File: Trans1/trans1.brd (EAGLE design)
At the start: 45.7 x 33 mm, 21 parts, among them Q1 MOSFET-NCHANNELBSS138, U1 DRA818V

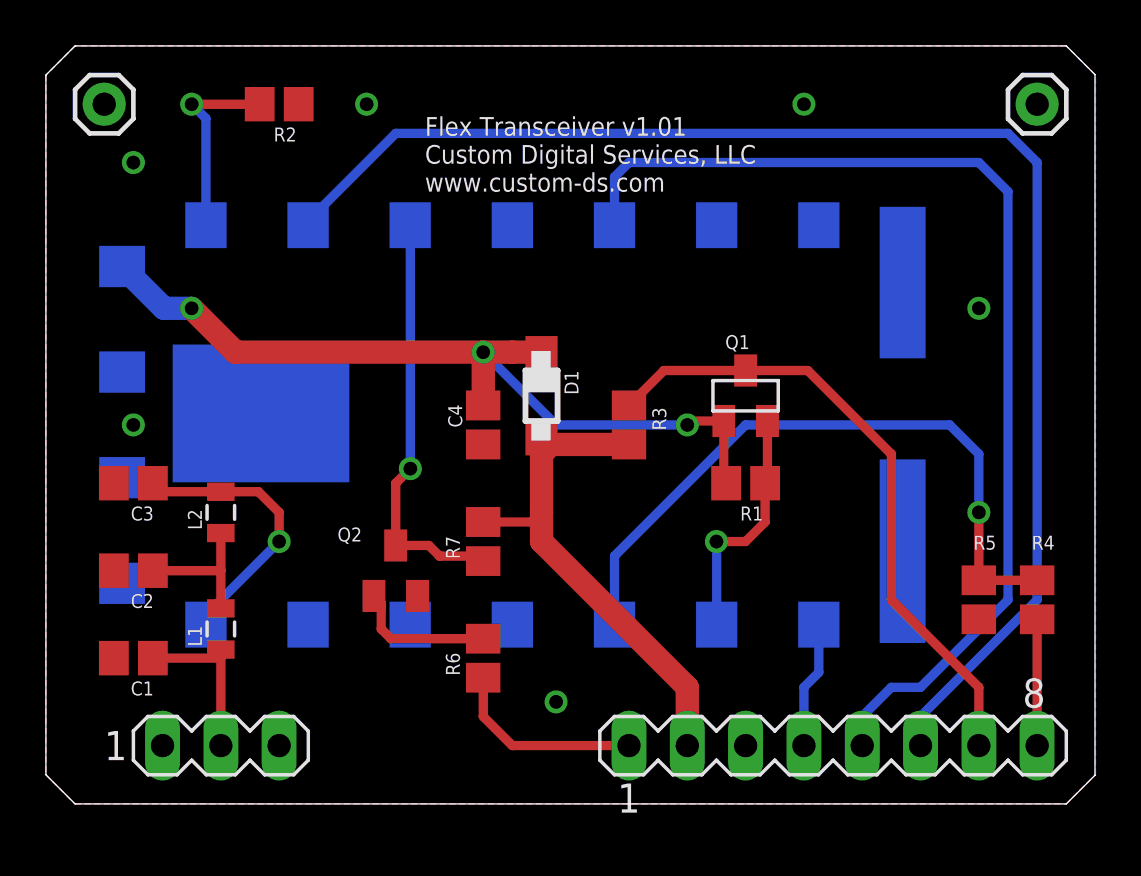
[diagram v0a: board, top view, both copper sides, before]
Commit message: Version 1.03
Added third pole to RF filter, adjusted pad size on DRA module.
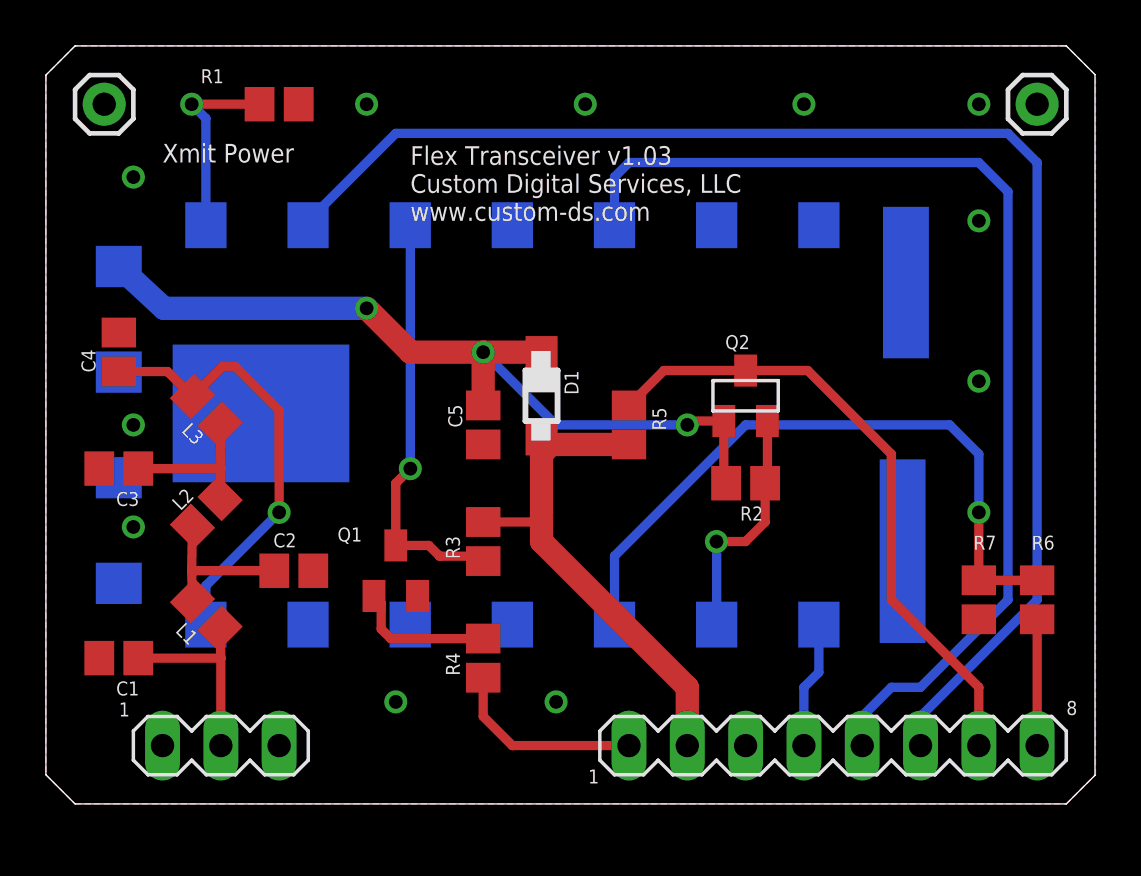
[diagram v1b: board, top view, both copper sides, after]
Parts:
- added C5: .1uF, resistor:C0805
- added L3: 1µH, custom-ds:L0805
- C1, C4: value (none) -> 20pF
- C2, C3: value (none) -> 36pF
- D1: value (none) -> 1N4148
- L1, L2: value (none) -> 1µH; device SparkFun-Passives:0805 -> custom-ds:L0805
- Q1: value MOSFET-NCHANNELBSS138 -> (none); device SparkFun-DiscreteSemi:SOT23 -> transistor-npn:SOT23-BEC
- Q2: value (none) -> MOSFET-NCHANNELBSS138; device transistor-npn:SOT23-BEC -> SparkFun-DiscreteSemi:SOT23
- R1, R2, R5, R6: value (none) -> 10k
- R3, R4: value (none) -> 1k
- R7: value (none) -> 100k
- U1: device DRA818V:SMD_DRA818 -> custom-ds:SMD_DRA818
- moved R1 26.2 mm to (10.2, 30.5)
- moved R2 26.2 mm to (30.5, 14.0)
- moved R4 24.3 mm to (19.1, 6.35)
- moved R6 24.3 mm to (43.2, 8.89)
- moved R7 21.7 mm to (40.6, 8.89)
- moved R5 17.0 mm to (25.4, 16.5), turned to 270 degrees
- moved Q1 17.0 mm to (15.2, 10.2)
- moved Q2 17.0 mm to (30.5, 17.8)
- moved C4 16.2 mm to (3.17, 19.7), turned to 90 degrees
- moved R3 8.13 mm to (19.1, 11.4), turned to 90 degrees
- moved C2 6.98 mm to (10.8, 10.2), turned to 0 degrees
- moved L1 0.90 mm to (6.99, 8.26), turned to 135 degrees
- moved C3 0.90 mm to (3.17, 14.6)
- moved C1 0.64 mm to (3.17, 6.35)
- moved L2 0.63 mm to (6.99, 12.7), turned to 45 degrees
- renumbered SV1 to J2, SV3 to J1
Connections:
- new net N$7: C3.1, L2.2, L3.1
- net +5V: now also R5.2; no longer R7.2
- net GND: now also C5.2, Q1.E, R1.1, R7.1; no longer Q2.E, R2.1, R5.1
- net N$1: now also Q1.C, R3.1; no longer Q2.C, R7.1
- net N$2: now also R1.2; no longer R2.2
- net N$3: now also R6.2, R7.2; no longer R4.2, R5.2
- net N$4: now also Q2.2, R2.1; no longer Q1.2, R1.1
- net N$5: now also Q1.B, R4.2; no longer Q2.B, R6.2
- net N$6: now also C4.1, L3.2; no longer C3.1, L2.2
- net PTT: now also R4.1; no longer R6.1
- net RX_DATA: now also Q2.3, R5.1; no longer Q1.3, R3.1
- net TX_DATA: now also R6.1; no longer R4.1
- net V+: now also C5.1, Q2.1, R2.2; no longer C4.1, Q1.1, R1.2
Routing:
- net N$6: track 12.2 -> 19.4 mm
- net N$7: track 0.00 -> 6.84 mm
- net N$10: track 7.14 -> 8.71 mm
- net N$9: track 6.24 -> 6.84 mm
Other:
- board text added: "Flex Transceiver v1.03 Custom Digital Services, LLC www.custom-ds.com"
- board text added: "Xmit Power"
- board text removed: "Flex Transceiver v1.01 Custom Digital Services, LLC www.custom-ds.com"

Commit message: Updating part values
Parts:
- L1, L3: value 1µH -> 56nH
- L2: value 1µH -> 68nH
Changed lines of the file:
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@@
 <element name="C3" library="resistor" package="C0805" value="36pF" x="3.175" y="14.605" smashed="yes" rot="R180">
 <attribute name="NAME" x="4.064" y="13.589" size="0.6096" layer="25" font="vector" rot="R180"/>
+<attribute name="DIGIKEY" value="478-10473-1-ND" x="3.175" y="14.605" size="1.778" layer="27" rot="R180" display="off"/>
 </element>
 <element name="C4" library="resistor" package="C0805" value="20pF" x="3.175" y="19.685" smashed="yes" rot="R90">
 <attribute name="NAME" x="2.159" y="18.796" size="0.6096" layer="25" font="vector" rot="R90"/>
+<attribute name="DIGIKEY" value="‎712-1381-1-ND‎" x="3.175" y="19.685" size="1.778" layer="27" rot="R90" display="off"/>
 </element>
 <element name="C2" library="resistor" package="C0805" value="36pF" x="10.795" y="10.16" smashed="yes">
 <attribute name="NAME" x="9.906" y="11.176" size="0.6096" layer="25" font="vector"/>
+<attribute name="DIGIKEY" value="478-10473-1-ND" x="10.795" y="10.16" size="1.778" layer="27" display="off"/>
 </element>
 <element name="C5" library="resistor" package="C0805" value=".1uF" x="19.05" y="16.51" smashed="yes" rot="R270">
@@
 <element name="JP1" library="SparkFun-Connectors" package="1X01" value="M01PTH" x="43.18" y="30.48" smashed="yes"/>
 <element name="JP2" library="SparkFun-Connectors" package="1X01" value="M01PTH" x="2.54" y="30.48" smashed="yes"/>
-<element name="L2" library="custom-ds" package="L0805" value="1µH" x="6.985" y="12.7" smashed="yes" rot="R45">
+<element name="L2" library="custom-ds" package="L0805" value="68nH" x="6.985" y="12.7" smashed="yes" rot="R45">
 <attribute name="NAME" x="5.862475" y="12.7449" size="0.6096" layer="25" font="vector" rot="R45"/>
 <attribute name="VALUE" value="1µH" x="7.254409375" y="10.99375" size="0.4064" layer="27" rot="R45" display="off"/>
+<attribute name="DIGIKEY" value="‎535-11572-1-ND‎" x="6.985" y="12.7" size="1.778" layer="27" rot="R45" display="off"/>
 </element>
-<element name="L3" library="custom-ds" package="L0805" value="1µH" x="6.985" y="17.145" smashed="yes" rot="R135">
+<element name="L3" library="custom-ds" package="L0805" value="56nH" x="6.985" y="17.145" smashed="yes" rot="R135">
 <attribute name="NAME" x="6.940096875" y="16.022465625" size="0.6096" layer="25" font="vector" rot="R135"/>
 <attribute name="VALUE" value="1µH" x="8.691246875" y="17.41440625" size="0.4064" layer="27" rot="R135" display="off"/>
+<attribute name="DIGIKEY" value="535-11570-1-ND" x="6.985" y="17.145" size="1.778" layer="27" rot="R135" display="off"/>
 </element>
 <element name="R1" library="resistor" package="R0805" value="10k" x="10.16" y="30.48" smashed="yes" rot="R180">
@@
 <attribute name="NAME" x="18.034" y="10.668" size="0.6096" layer="25" font="vector" rot="R90"/>
 </element>
-<element name="L1" library="custom-ds" package="L0805" value="1µH" x="6.985" y="8.255" smashed="yes" rot="R135">
+<element name="L1" library="custom-ds" package="L0805" value="56nH" x="6.985" y="8.255" smashed="yes" rot="R135">
 <attribute name="NAME" x="6.35638125" y="7.62638125" size="0.6096" layer="25" font="vector" rot="R135" align="bottom-center"/>
+<attribute name="DIGIKEY" value="535-11570-1-ND" x="6.985" y="8.255" size="1.778" layer="27" rot="R135" display="off"/>
 </element>
 <element name="C1" library="resistor" package="C0805" value="20pF" x="3.175" y="6.35" smashed="yes" rot="R180">
 <attribute name="NAME" x="4.064" y="5.334" size="0.6096" layer="25" rot="R180"/>
+<attribute name="DIGIKEY" value="‎712-1381-1-ND‎" x="3.175" y="6.35" size="1.778" layer="27" rot="R180" display="off"/>
 </element>
 </elements>
